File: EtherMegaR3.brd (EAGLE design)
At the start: 125 x 69 mm, 49 parts, among them IC2 APX811-44UG-7, IC4 MCP24AA025E48, IC6 W5100SQFP80, IC9 ATMEGA2560-16AU, Q3 2N7002, U1 HY931147C-RJ45, X2 25MHz, X3 16MHz

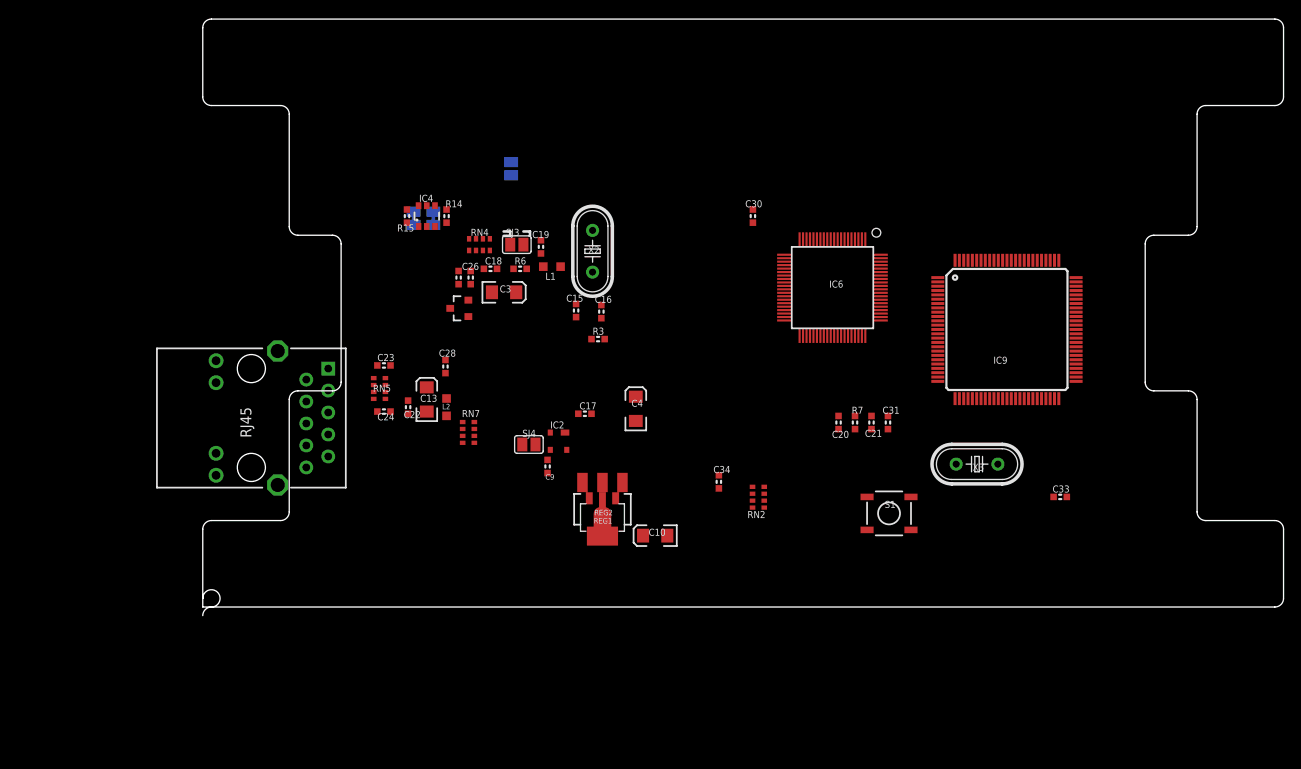
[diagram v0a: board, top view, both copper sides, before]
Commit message: remove eagle.epf
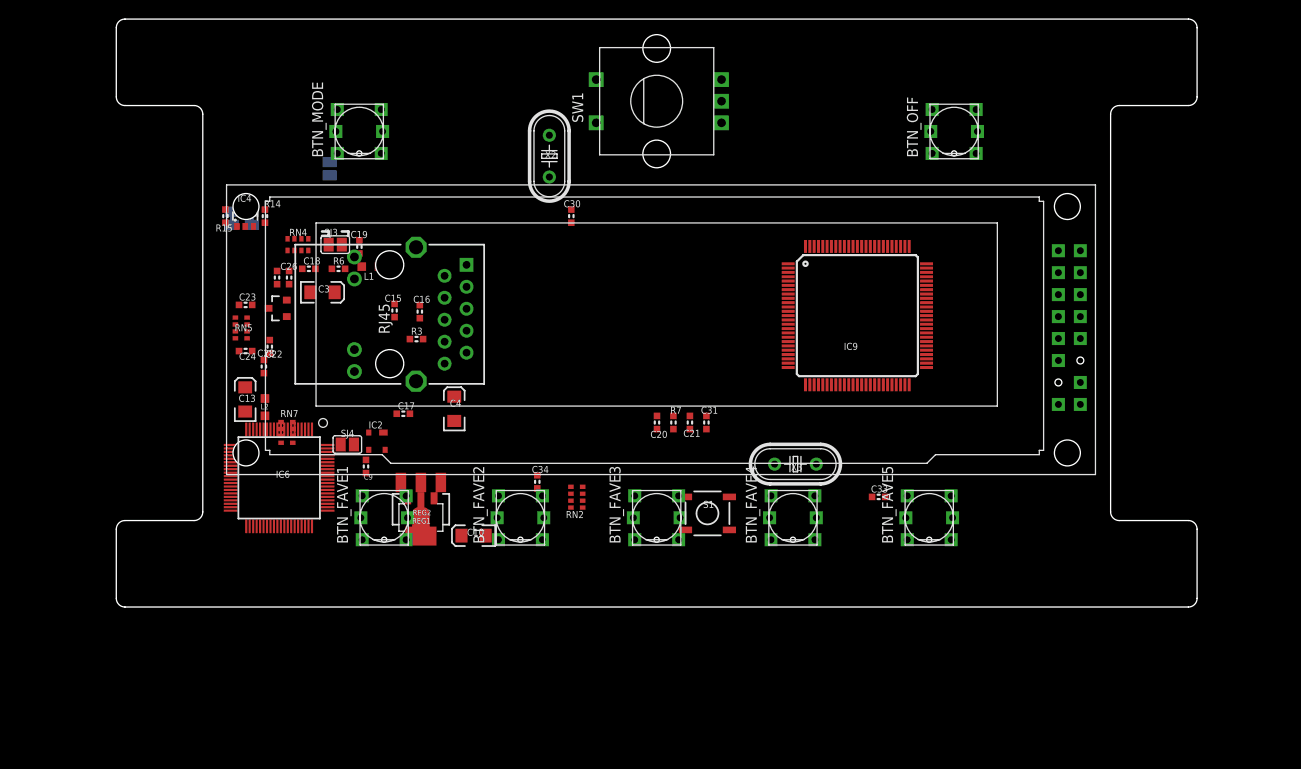
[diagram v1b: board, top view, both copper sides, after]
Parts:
- added BTN_FAVE1, BTN_FAVE2, BTN_FAVE3, BTN_FAVE4, BTN_FAVE5, BTN_MODE, BTN_OFF: PB614, RSJ-PB614:PB614
- added SW1: EC12E_SW, switch-alps:ALPS_EC12E_SW
- added U$1: ER-OLED-M032-1W, Mat-Library:ER-OLED-M032-1W
- moved IC6 67.7 mm to (8.83, 14.9)
- moved C31 21.0 mm to (58.2, 21.3)
- moved IC2 21.0 mm to (20.1, 19.2)
- moved L1 21.0 mm to (19.4, 39.4)
- moved R6 21.0 mm to (15.7, 39.1)
- moved SJ3 21.0 mm to (15.3, 41.9)
- moved C13 21.0 mm to (4.91, 24.0)
- moved C15 21.0 mm to (22.2, 34.3)
- moved C16 21.0 mm to (25.1, 34.2)
- moved C18 21.0 mm to (12.3, 39.1)
- moved C19 21.0 mm to (18.1, 41.7)
- moved C20 21.0 mm to (52.5, 21.3)
- moved C21 21.0 mm to (56.3, 21.3)
- moved C25 21.0 mm to (8.59, 38.1)
- moved C26 21.0 mm to (9.99, 38.1)
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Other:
- board size 125 x 69 mm -> 125 x 68 mm

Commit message: - Finished placing physical dimensions (button holes, faceplate outlines) - Added Fleetwood components - Added signal level converter (based on Sparkfun bi-directional converter) - Removed REG1 in 3v3 power supply as we will use only the bigger SOT223 one - Placed WIZNET and ATMEGA chips and most of their associated components onto relevant side of board - Positioned Fleetwood components - Have not yet included MPR121 cap sense - Have not yet positioned WIZNET and ATMEGA chips and components in proper locations
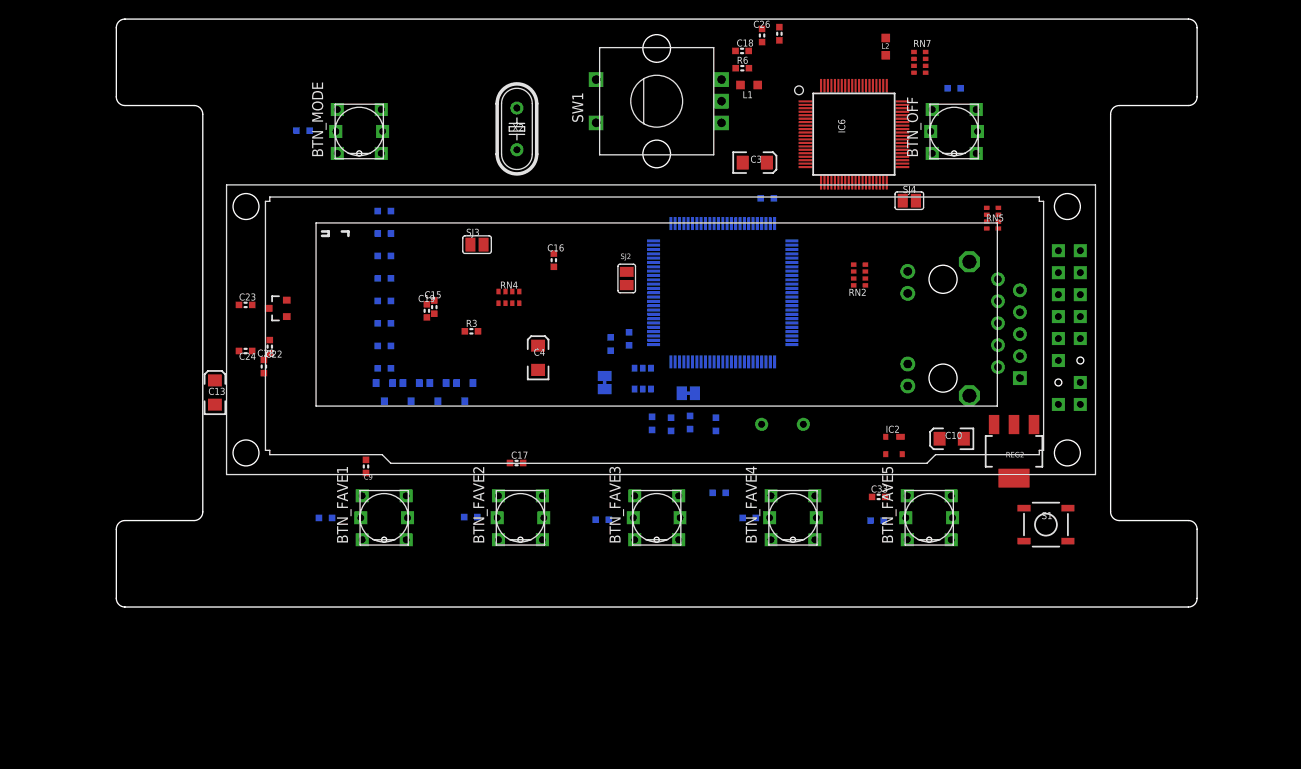
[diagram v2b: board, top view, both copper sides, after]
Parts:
- removed REG1: LD1117-SOT89, freetronics:SOT89
- added OLED_CLK, OLED_CS, OLED_DATA, OLED_DS: BSS138, SparkFun:SOT23-3
- added R20, R21, R22, R23, R24, R25, R26, R27: 10k, freetronics-marc:0603
- added R28, R29, R30, R31, R32, R33, R34: 100R, freetronics-marc:0603
- moved RN5 87.8 mm to (91.3, 45.0)
- moved RN7 84.8 mm to (82.9, 63.0)
- moved L2 83.0 mm to (79.0, 64.8)
- moved IC6 77.5 mm to (75.3, 54.7), turned to 0 degrees
- moved SJ4 70.9 mm to (81.7, 47.0)
- moved REG2 68.9 mm to (93.8, 18.0)
- moved C25 64.6 mm to (66.7, 66.3)
- moved U1 64.0 mm to (85.6, 32.2), flipped to the bottom, turned to 180 degrees
- moved C26 61.4 mm to (64.7, 66.1)
- moved IC2 59.8 mm to (79.9, 18.7)
- moved C10 56.4 mm to (86.6, 19.5)
- moved C18 56.1 mm to (62.4, 64.3)
- moved SJ5 54.4 mm to (56.2, 24.7), turned to 0 degrees
- moved C3 52.2 mm to (63.8, 51.4)
- moved R6 52.1 mm to (62.4, 62.3)
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- renumbered U$1 to OLED
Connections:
- new net ADC8: BTN_FAVE5.1
- new net ADC9: BTN_FAVE5.L+
- new net N$10: BTN_FAVE4.L-, R31.2
- new net N$11: BTN_FAVE5.L-, R32.2
- new net N$12: BTN_MODE.L-, R33.2
- new net N$13: BTN_OFF.L-, R34.2
- new net N$2: BTN_FAVE1.L-, R28.2
- new net N$3: OLED.4, OLED_CLK.2, R20.1
- new net N$4: OLED.5, OLED_DATA.2, R22.1
- new net N$5: BTN_FAVE2.L-, R29.2
- new net N$6: OLED.14, OLED_DS.2, R24.1
- new net N$7: BTN_FAVE3.L-, R30.2
- new net N$8: OLED.16, OLED_CS.2, R26.1
- net 3V3D: now also R20.2, R22.2, R24.2, R26.2; no longer REG1.2, REG1.4
- net 5V: now also OLED.15, OLED.2, R21.2, R23.2, R25.2, R27.2; no longer REG1.3
- net A10: now also BTN_MODE.1
- net A11: now also BTN_MODE.L+
- net A13: now also BTN_OFF.1
- net A14: now also BTN_OFF.L+
- net ADC0: now also BTN_FAVE1.1
- net ADC1: now also BTN_FAVE1.L+
- net ADC2: now also BTN_FAVE2.1
- net ADC3: now also BTN_FAVE2.L+
- net ADC4: now also BTN_FAVE3.1
- net ADC5: now also BTN_FAVE3.L+
- net ADC6: now also BTN_FAVE4.1
- net ADC7: now also BTN_FAVE4.L+
- net D2: now also SW1.A
- net D3: now also SW1.B
- net D4: now also OLED_CLK.3, R21.1
- net D5: now also OLED_DATA.3, R23.1
- net D6: now also OLED_CS.3, R27.1
- net D7: now also OLED_DS.3, R25.1
- net D8: now also SW1.D
- net GND: now also BTN_FAVE1.4, BTN_FAVE2.4, BTN_FAVE3.4, BTN_FAVE4.4, BTN_FAVE5.4, BTN_MODE.4, BTN_OFF.4, OLED.1, OLED.10, OLED.11, OLED.12, OLED.13, OLED.7, OLED.8, OLED.9, R28.1, R29.1, R30.1, R31.1, R32.1, R33.1, R34.1, SW1.C, SW1.E; no longer REG1.1
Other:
- board text removed: "A"
- board text removed: "K"

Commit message: minor eagle updates
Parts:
- removed RN2: 1K, freetronics-master-v1:CAY16
- added RN2A, RN2B: 1k, freetronics-marc:0603
- added U$1: EUP3476SO08T, freetronics-jon:SO08T
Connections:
- new net IN: U$1.2
- new net TGND: U$1.9
- net FDXLED: now also RN2A.1; no longer RN2.8
- net GND: now also U$1.4
- net LINKLED: now also RN2B.1; no longer RN2.7
- net N$332: now also RN2B.2; no longer RN2.2
- net N$67: now also RN2A.2; no longer RN2.1
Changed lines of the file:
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@@
 <attribute name="VALUE" x="55.305" y="22.152" size="0.635" layer="28" font="vector" ratio="17" rot="MR270"/>
-</element>
-<element name="RN2" library="freetronics-master-v1" package="CAY16" value="1K" x="75.962" y="38.4" smashed="yes" rot="R270">
-<attribute name="NAME" x="74.692" y="35.987" size="0.8128" layer="25" ratio="17"/>
-<attribute name="VALUE" x="77.232" y="40.305" size="0.635" layer="27" ratio="17" rot="R270"/>
 </element>
 <element name="RN5" library="freetronics-master-v1" package="CAY16" value="49R9 1%" x="91.347" y="44.973" smashed="yes" rot="R270">
@@
 <element name="R33" library="freetronics-marc" package="0603" value="100R" x="11.6" y="55.1" rot="MR0"/>
 <element name="R34" library="freetronics-marc" package="0603" value="100R" x="86.9" y="60" rot="MR0"/>
+<element name="RN2A" library="freetronics-marc" package="0603" value="1k" x="72.8" y="39.1"/>
+<element name="RN2B" library="freetronics-marc" package="0603" value="1k" x="72.8" y="36.4"/>
+<element name="U$1" library="freetronics-jon" package="SO08T" value="EUP3476SO08T" x="-17.9" y="-14.5"/>
 </elements>
 <signals>
@@
 <contactref element="BTN_OFF" pad="4"/>
 <contactref element="BTN_MODE" pad="4"/>
-<wire x1="80.91" y1="56.08" x2="89.44" y2="57.54" width="0" layer="19" extent="1-1"/>
+<contactref element="U$1" pad="4"/>
+<wire x1="89.44" y1="57.54" x2="87.662" y2="60" width="0" layer="19" extent="16-16"/>
+<wire x1="80.91" y1="56.08" x2="87.662" y2="60" width="0" layer="19" extent="1-16"/>
 <wire x1="80.91" y1="55.68" x2="80.91" y2="56.08" width="0" layer="19" extent="1-1"/>
 <wire x1="80.91" y1="55.28" x2="80.91" y2="55.68" width="0" layer="19" extent="1-1"/>
@@
 <wire x1="58.96" y1="13.21" x2="56.357" y2="20.574" width="0" layer="19" extent="16-16"/>
 <wire x1="55.04" y1="12.86" x2="58.96" y2="13.21" width="0" layer="19" extent="16-16"/>
-<wire x1="40.601" y1="40.875" x2="49.032" y2="37.2364" width="0" layer="19" extent="1-1"/>
-<wire x1="38.785" y1="27.423" x2="49.942" y2="27.612" width="0" layer="19" extent="1-16"/>
-<wire x1="37.058" y1="16.652" x2="38.785" y2="27.423" width="0" layer="19" extent="1-1"/>
-<wire x1="39.28" y1="12.86" x2="37.058" y2="16.652" width="0" layer="19" extent="1-1"/>
-<wire x1="30.238" y1="10.4" x2="37.058" y2="16.652" width="0" layer="19" extent="1-16"/>
-<wire x1="46.962" y1="10.1" x2="30.238" y2="10.4" width="0" layer="19" extent="1-16"/>
-<wire x1="63.962" y1="10.3" x2="46.962" y2="10.1" width="0" layer="19" extent="1-1"/>
-<wire x1="78.762" y1="10" x2="63.962" y2="10.3" width="0" layer="19" extent="1-1"/>
-<wire x1="12.362" y1="55.1" x2="78.762" y2="10" width="0" layer="19" extent="1-1"/>
-<wire x1="87.662" y1="60" x2="12.362" y2="55.1" width="0" layer="19" extent="1-1"/>
-<wire x1="23.52" y1="12.86" x2="30.238" y2="10.4" width="0" layer="19" extent="16-16"/>
-<wire x1="18.878" y1="17.018" x2="23.52" y2="12.86" width="0" layer="19" extent="1-1"/>
-<wire x1="13.438" y1="10.3" x2="18.878" y2="17.018" width="0" layer="19" extent="1-16"/>
-<wire x1="70.8" y1="12.86" x2="58.96" y2="13.21" width="0" layer="19" extent="16-16"/>
+<wire x1="63.962" y1="10.3" x2="58.96" y2="13.21" width="0" layer="19" extent="16-16"/>
+<wire x1="70.8" y1="12.86" x2="63.962" y2="10.3" width="0" layer="19" extent="16-16"/>
 <wire x1="78.932" y1="12.736" x2="70.8" y2="12.86" width="0" layer="19" extent="1-1"/>
+<wire x1="78.762" y1="10" x2="78.932" y2="12.736" width="0" layer="19" extent="1-16"/>
 <wire x1="80.698" y1="19.677" x2="78.932" y2="12.736" width="0" layer="19" extent="1-1"/>
 <wire x1="88.024" y1="19.455" x2="80.698" y2="19.677" width="0" layer="19" extent="1-1"/>
@@
 <wire x1="94.982" y1="11.432" x2="86.56" y2="12.86" width="0" layer="19" extent="1-1"/>
 <wire x1="100.062" y1="11.432" x2="94.982" y2="11.432" width="0" layer="19" extent="1-1"/>
+<wire x1="46.962" y1="10.1" x2="55.04" y2="12.86" width="0" layer="19" extent="16-16"/>
+<wire x1="39.28" y1="12.86" x2="46.962" y2="10.1" width="0" layer="19" extent="16-16"/>
+<wire x1="37.058" y1="16.652" x2="39.28" y2="12.86" width="0" layer="19" extent="1-1"/>
+<wire x1="40.601" y1="40.875" x2="49.032" y2="37.2364" width="0" layer="19" extent="1-1"/>
+<wire x1="30.238" y1="10.4" x2="37.058" y2="16.652" width="0" layer="19" extent="1-16"/>
+<wire x1="23.52" y1="12.86" x2="30.238" y2="10.4" width="0" layer="19" extent="16-16"/>
+<wire x1="18.878" y1="17.018" x2="23.52" y2="12.86" width="0" layer="19" extent="1-1"/>
+<wire x1="13.438" y1="10.3" x2="18.878" y2="17.018" width="0" layer="19" extent="1-16"/>
 <wire x1="88.67" y1="39.935" x2="98.96" y2="38.67" width="0" layer="19" extent="1-1"/>
+<wire x1="38.785" y1="27.423" x2="37.058" y2="16.652" width="0" layer="19" extent="1-1"/>
 <wire x1="26.78" y1="35.452" x2="38.785" y2="27.423" width="0" layer="19" extent="1-1"/>
 <wire x1="45.5" y1="61" x2="60" y2="58.5" width="0" layer="19" extent="1-1"/>
@@
 <wire x1="9.718" y1="35.494" x2="4.193" y2="34.94" width="0" layer="19" extent="1-1"/>
 <wire x1="1.408" y1="23.403" x2="4.193" y2="29.606" width="0" layer="19" extent="1-1"/>
-<wire x1="20.64" y1="57.54" x2="26.78" y2="35.452" width="0" layer="19" extent="1-1"/>
+<wire x1="12.362" y1="55.1" x2="9.718" y2="35.494" width="0" layer="19" extent="1-16"/>
+<wire x1="20.64" y1="57.54" x2="12.362" y2="55.1" width="0" layer="19" extent="16-16"/>
+<wire x1="-20.5" y1="-16.405" x2="13.438" y2="10.3" width="0" layer="19" extent="1-16"/>
 </signal>
 <signal name="TXOP">
@@
 <signal name="LINKLED">
 <contactref element="IC6" pad="66"/>
-<contactref element="RN2" pad="7"/>
-<wire x1="76.637" y1="38.8" x2="77.11" y2="60.28" width="0" layer="19" extent="1-1"/>
+<contactref element="RN2B" pad="1"/>
+<wire x1="72.038" y1="36.4" x2="77.11" y2="60.28" width="0" layer="19" extent="1-1"/>
 </signal>
 <signal name="N$322">
@@
 <signal name="FDXLED">
 <contactref element="IC6" pad="70"/>
-<contactref element="RN2" pad="8"/>
-<wire x1="76.637" y1="39.6" x2="75.51" y2="60.28" width="0" layer="19" extent="1-1"/>
+<contactref element="RN2A" pad="1"/>
+<wire x1="72.038" y1="39.1" x2="75.51" y2="60.28" width="0" layer="19" extent="1-1"/>
 </signal>
 <signal name="XTLP">
@@
 <signal name="N$332">
 <contactref element="U1" pad="P$12"/>
-<contactref element="RN2" pad="2"/>
-<wire x1="81.54" y1="28.105" x2="75.287" y2="38.8" width="0" layer="19" extent="1-1"/>
+<contactref element="RN2B" pad="2"/>
+<wire x1="73.562" y1="36.4" x2="81.54" y2="28.105" width="0" layer="19" extent="1-1"/>
 </signal>
 <signal name="TXON">
@@
 <signal name="N$67">
 <contactref element="U1" pad="P$14"/>
-<contactref element="RN2" pad="1"/>
-<wire x1="75.287" y1="39.6" x2="81.54" y2="38.815" width="0" layer="19" extent="1-1"/>
+<contactref element="RN2A" pad="2"/>
+<wire x1="73.562" y1="39.1" x2="81.54" y2="38.815" width="0" layer="19" extent="1-1"/>
 </signal>
 <signal name="N$68">
@@
 <wire x1="86.138" y1="60" x2="84.2" y2="55" width="0" layer="19" extent="1-1"/>
 </signal>
+<signal name="IN">
+<contactref element="U$1" pad="2"/>
+</signal>
+<signal name="TGND">
+<contactref element="U$1" pad="9"/>
+</signal>
 </signals>
